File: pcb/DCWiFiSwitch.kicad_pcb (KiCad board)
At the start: 2 copper layers, 50 x 50 mm, 47 parts, among them J1 Screw_Terminal_01x06, J2 Conn_01x06, Q1 AO3400A, Q2 AO3400A, SW1 SW1_BOOT, U1 TPS5430DDA, U2 EL817, U3 EL817, U4 ESP-12F

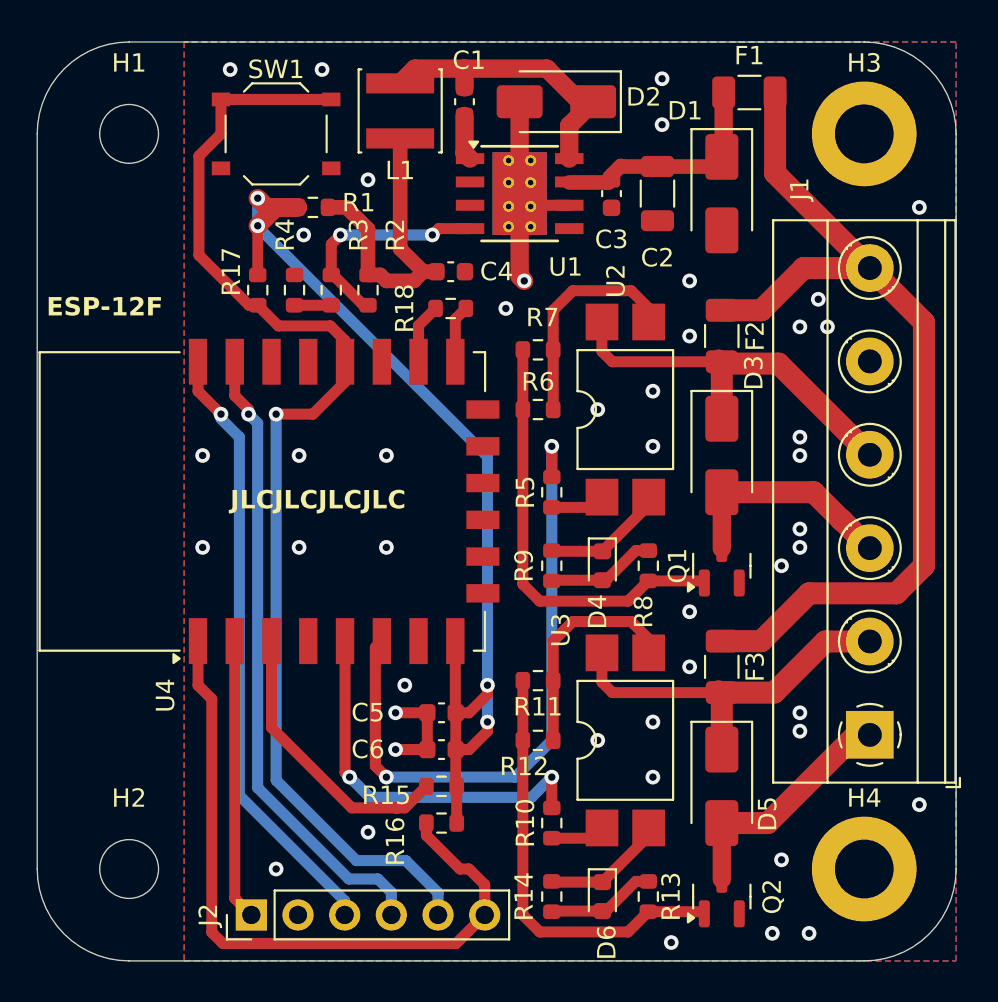
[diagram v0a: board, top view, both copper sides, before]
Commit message: add 3v3 to the pinheader, tweaked board
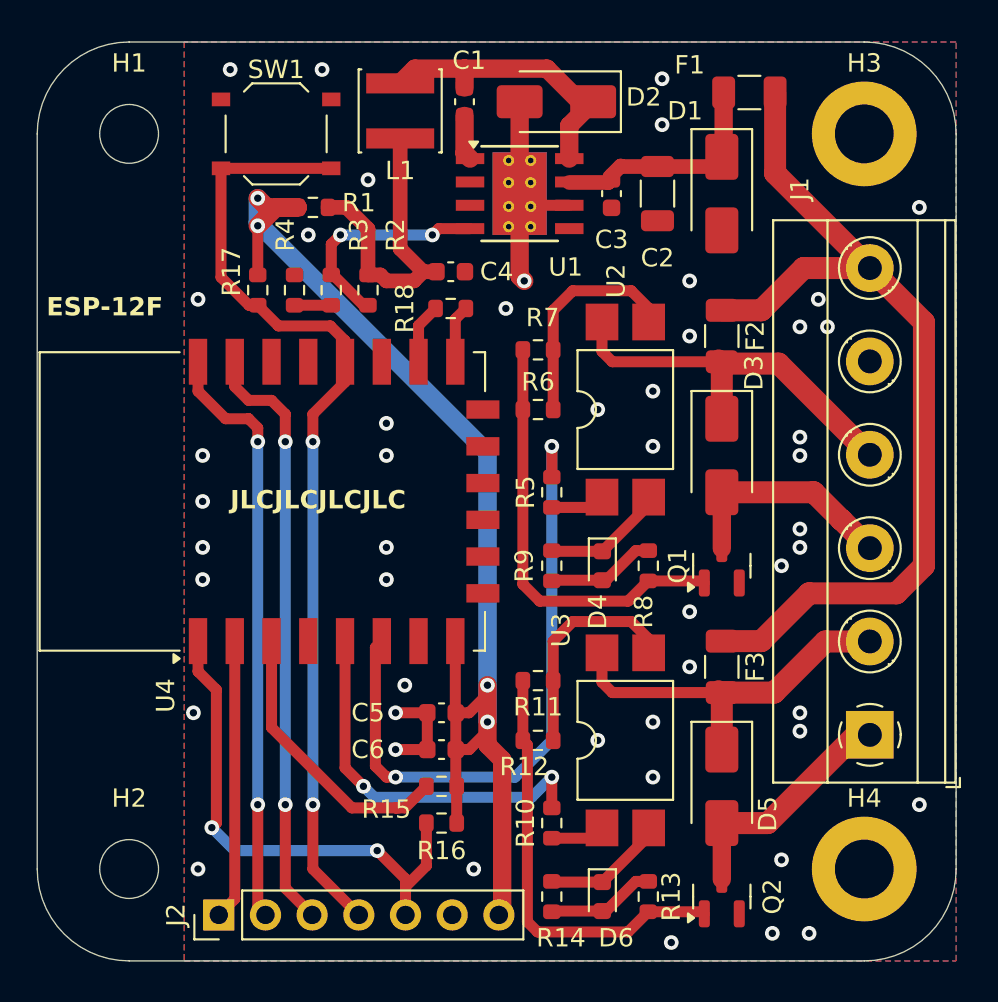
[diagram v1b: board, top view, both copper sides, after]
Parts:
- J2: value Conn_01x06 -> Conn_01x07; footprint Connector_PinHeader_2.54mm:PinHeader_1x06_P2.54mm_Vertical -> Connector_PinHeader_2.54mm:PinHeader_1x07_P2.54mm_Vertical
- moved J2 1.77 mm to (99.9, 87.5)
- turned SW1 to 180 degrees
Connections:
- J2 pad 2: GND -> TXD
- J2 pad 3: TXD -> RXD
- J2 pad 4: RXD -> BOOT
- J2 pad 5: BOOT -> NRST
- J2 pad 6: NRST -> GND
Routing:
- net +3V3: track 56.5 -> 69.5 mm
- net BOOT: track 64.0 -> 53.1 mm, vias 1 -> 2
- net NRST: track 38.5 -> 28.3 mm, vias 0 -> 2
- net RXD: track 34.6 -> 32.6 mm, vias 1 -> 2
- net TXD: track 33.4 -> 32.4 mm, vias 1 -> 2
- net GND: vias 45 -> 49
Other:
- board text added: "3V3"

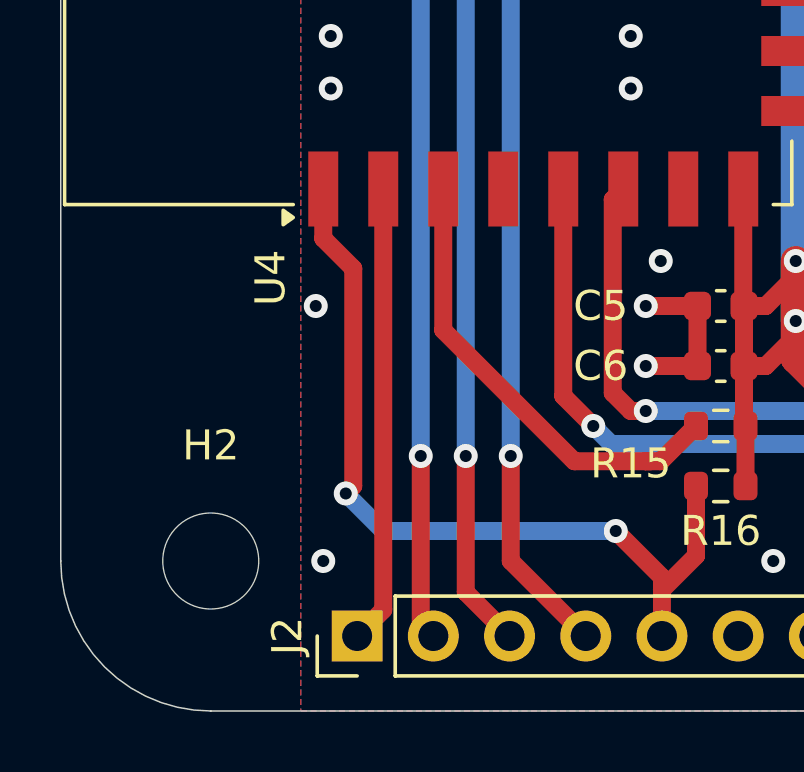
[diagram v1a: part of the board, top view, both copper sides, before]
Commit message: add adc resistor divider
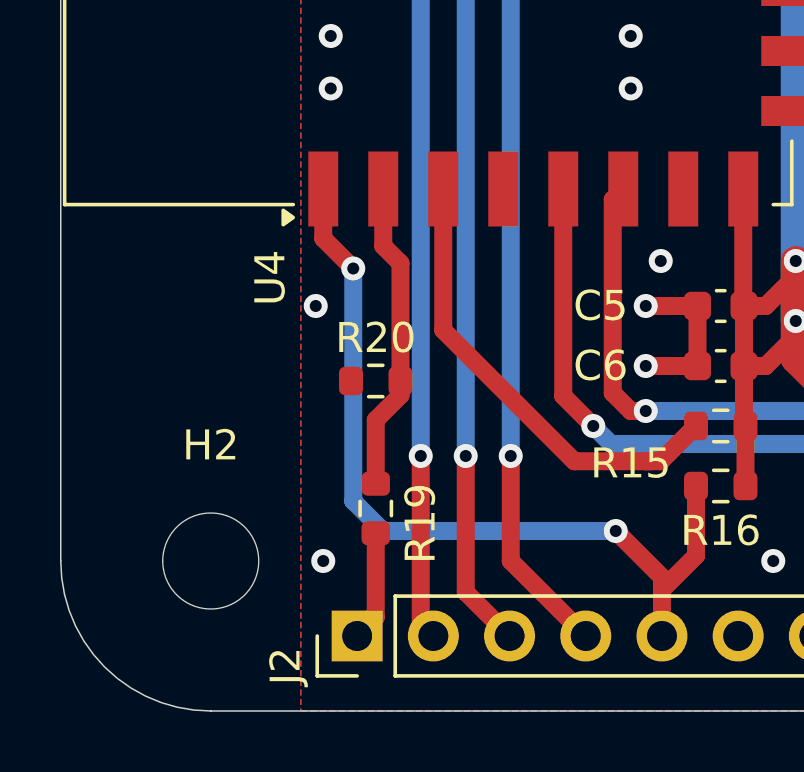
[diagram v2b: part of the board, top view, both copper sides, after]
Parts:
- added R19: 220k, Resistor_SMD:R_0603_1608Metric, F.Cu at (100.5, 83.2)
- added R20: 100k, Resistor_SMD:R_0603_1608Metric, F.Cu at (100.5, 79.0)
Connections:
- U4 pad 2: ADC -> Net-(U4-ADC)
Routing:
- net ADC: track 15.3 -> 3.68 mm
- net Net-(U4-ADC): track 0.00 -> 10.4 mm
